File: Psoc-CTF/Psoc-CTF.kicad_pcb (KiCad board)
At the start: 2 copper layers, 100 x 105.9 mm, 140 parts, among them IC1 CY8C4248LQI-BL583, J1 Conn_01x02, J10 Conn_01x20, J11 Conn_01x20, J12 USB3076-XX-X_REVC, J2 Conn_01x03, J3 Prog, J4 Conn_01x04, J5 USB3076-XX-X_REVC, J6 Conn_01x10, J7 Conn_01x04, J8 Conn_01x20, J9 Conn_01x20, P1 Power, P2 Analog, P3 Digital, P4 Digital, SW1 FSM4JSMATR, SW2 FSM4JSMATR, SW3 FSM4JSMATR, SW4 FSM4JSMATR, SW5 FSM4JSMATR, U1 AMS1117-5.0, U2 AMS1117-3.3, U3 ESP32-WROOM-32D, U4 FM24C04B-GTR, U5 CY7C65211-24LTXI, U6 AMS1117-3.3, U7 CY7C65211-24LTXI, Y1 24MHz, Y2 32.768Khz

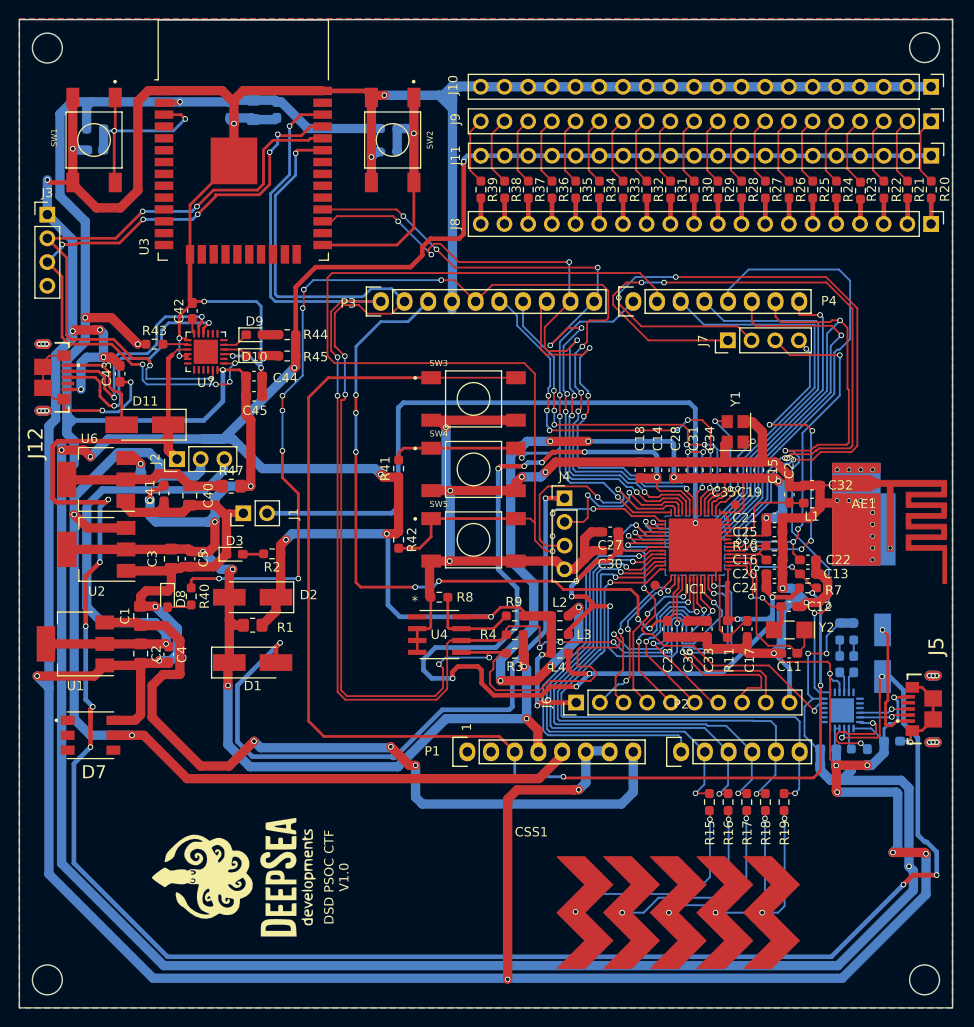
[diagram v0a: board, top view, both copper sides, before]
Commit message: Correcciones del retorno de tiera y medicion de corriente
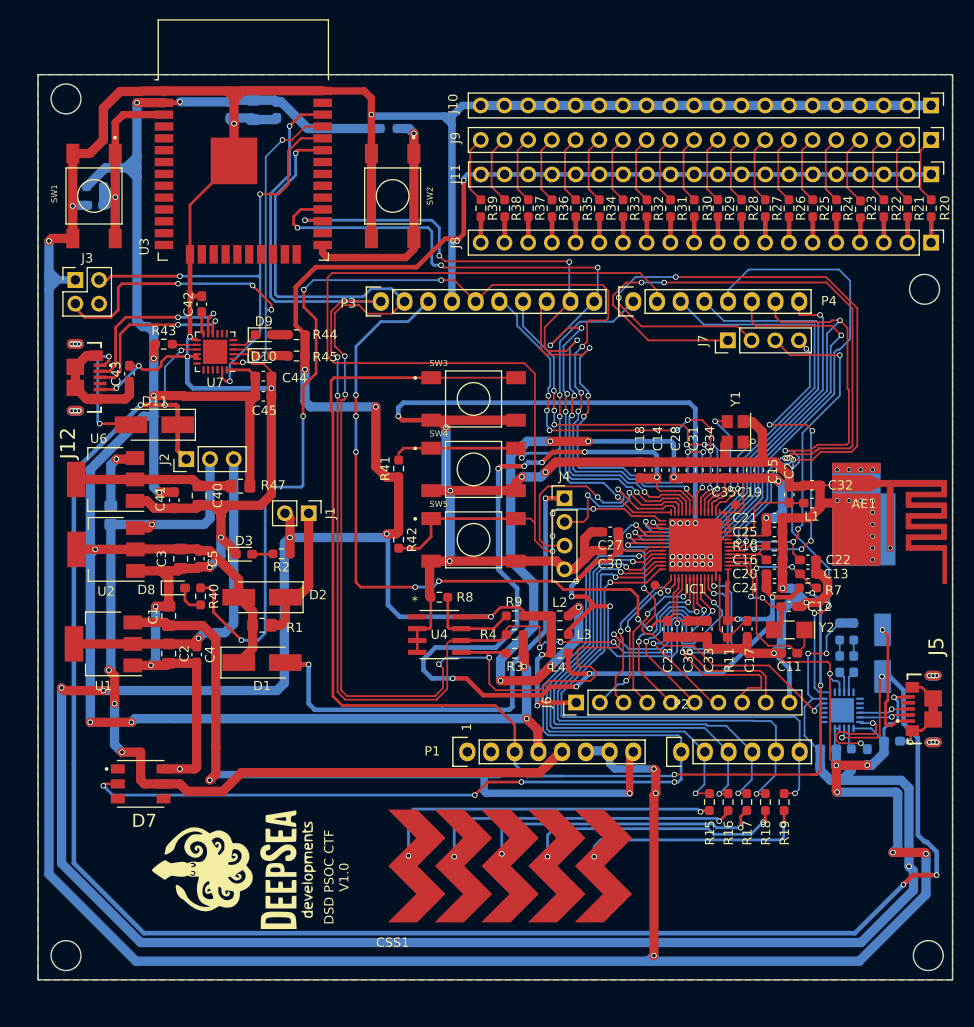
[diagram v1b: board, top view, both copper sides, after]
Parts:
- J3: footprint Connector_PinHeader_2.54mm:PinHeader_1x04_P2.54mm_Vertical -> Connector_PinHeader_2.54mm:PinHeader_2x02_P2.54mm_Vertical
- moved CSS1 18.7 mm to (154.6, 134.2)
- moved J3 7.62 mm to (117.0, 68.4)
- moved D7 7.49 mm to (124.0, 122.4)
- moved J1 7.00 mm to (142.0, 93.4), turned to 270 degrees
- moved R5 6.17 mm to (119.1, 58.4)
- moved SW1 6.00 mm to (119.0, 59.4)
- moved SW2 6.00 mm to (151.0, 59.4)
- moved R46 5.94 mm to (120.8, 93.6), turned to 270 degrees
- moved C9 5.92 mm to (119.1, 60.4)
- moved J12 3.46 mm to (117.0, 78.8)
- moved C1 3.00 mm to (127.0, 104.4)
- moved C2 3.00 mm to (127.0, 108.4)
- moved U1 3.00 mm to (120.0, 107.4)
- moved C4 3.00 mm to (130.0, 108.5)
- moved J10 2.00 mm to (208.7, 49.7)
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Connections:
- D2 pad 1: VDD -> VCC
- D7 pad 2: /MCU_Target/LED_RGB_DATA -> P2.0
- IC1 pad 11: GND1 -> GND
- IC1 pad 13: GND1 -> GND
- IC1 pad 55: GND1 -> GND
- IC1 pad 57: GND1 -> GND
- IC1 pad 9: GND1 -> GND
- J1 pad 1: GND -> VCC
- J1 pad 2: GND1 -> VDD
- R1 pad 1: VDD -> VCC
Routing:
- net GND1: track 87.0 -> 0.00 mm, vias 1 -> 0
- net P2.0: track 45.5 -> 113.1 mm, vias 1 -> 5
- net GND: track 767.0 -> 820.7 mm, vias 48 -> 63
- net VDD: track 403.2 -> 375.8 mm
- net /MCU_Target/3V3SWD: track 73.1 -> 54.9 mm
- net /power_supply/5VExt: track 52.5 -> 36.3 mm
- net /MONITOR/TXD: track 68.2 -> 52.3 mm, vias 4 -> 3
- net VCC: track 0.00 -> 15.0 mm
- net Net-(CSS1-Pad1): track 23.2 -> 37.3 mm
- net Net-(CSS1-Pad3): track 17.7 -> 31.2 mm
- net Net-(CSS1-Pad2): track 20.6 -> 34.0 mm
- net Net-(CSS1-Pad4): track 15.2 -> 27.8 mm
- net /MONITOR/RXD: track 71.9 -> 59.7 mm, vias 9 -> 5
- net Net-(CSS1-Pad5): track 13.0 -> 24.7 mm
- net /MCU_Target/VBUS: track 216.5 -> 205.3 mm, vias 9 -> 7
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- removed copper zone on B.Cu, net GND1
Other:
- board size 100 x 105.9 mm -> 98 x 97 mm

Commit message: Generacion de gerbers corregidos
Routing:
- net GND: vias 63 -> 65
